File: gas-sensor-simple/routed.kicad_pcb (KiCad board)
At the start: 2 copper layers, 91.4 x 99.1 mm, 43 parts, among them J1 2x5 pin, J2 2x5 socket, J3 2x5 pin, J4 1x2, J5 1x2, J6 1x2, J7 1x2, U1 MQ-8, U10 RG LED, U12 LM393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

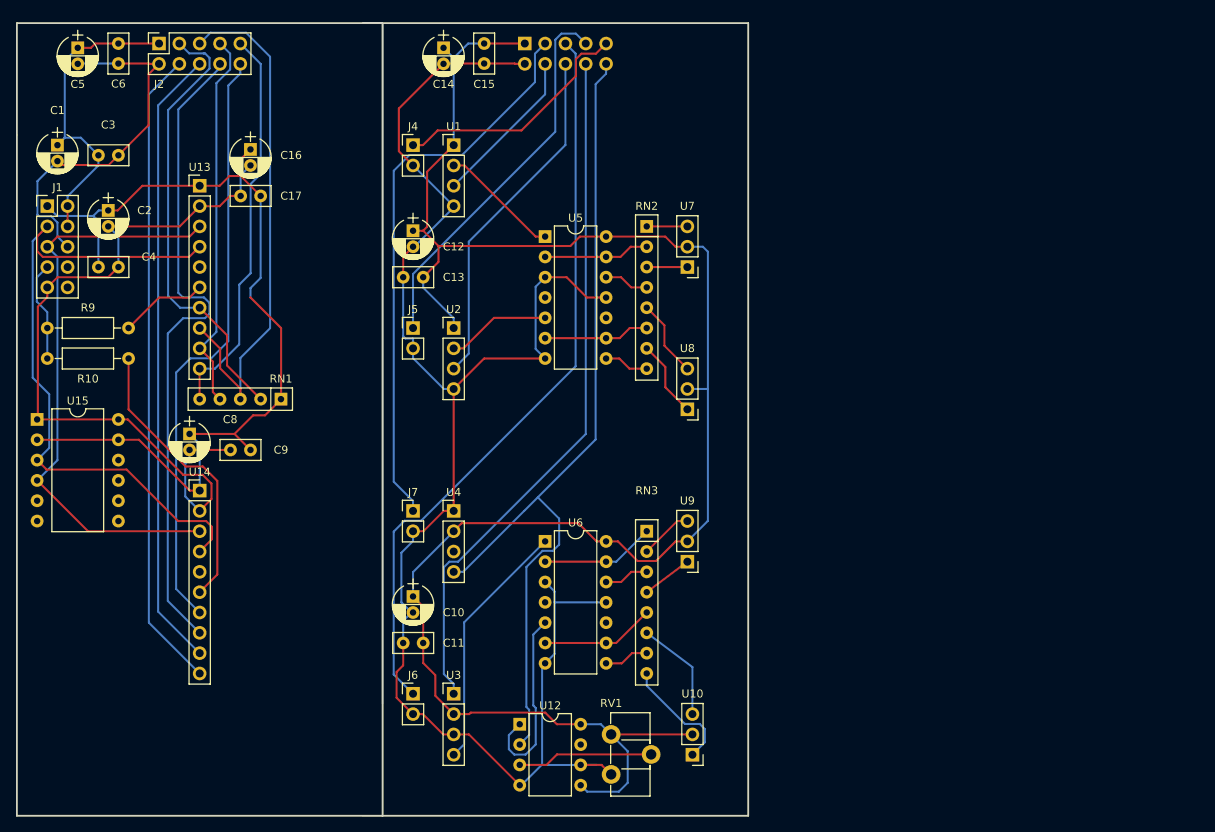
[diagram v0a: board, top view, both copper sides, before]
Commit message: Autorouted version 1 (gas-sensor-simple.kicad_pcb). Start work on version 2 layout (layout.kicad_pcb) moving RPi connector to top of digital board.
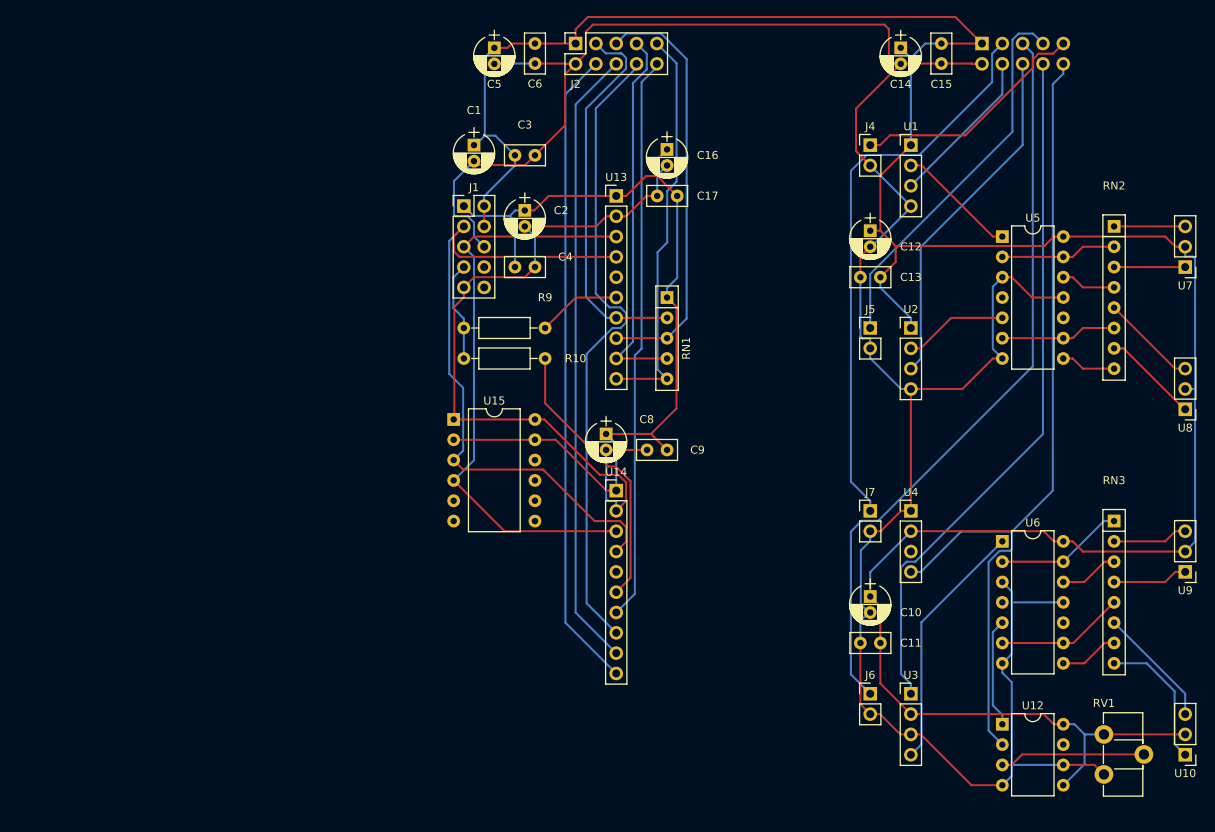
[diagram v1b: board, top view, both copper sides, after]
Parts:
- J1: value 2x5 pin -> RPi
- J2: value 2x5 socket -> digital header
- J3: value 2x5 pin -> digital header
- moved U9 62.2 mm to (248.9, 119.4)
- moved U7 62.2 mm to (248.9, 81.3)
- moved U8 62.2 mm to (248.9, 99.1)
- moved RV1 61.6 mm to (238.8, 139.7)
- moved U10 61.6 mm to (248.9, 142.2)
- moved U12 60.3 mm to (226.1, 138.4)
- moved RN3 58.4 mm to (240.0, 113.0)
- moved RN2 58.4 mm to (240.0, 76.2)
- moved C10 57.2 mm to (209.6, 122.5)
- moved C11 57.2 mm to (208.3, 128.3)
- moved C12 57.2 mm to (209.6, 76.7)
- moved C13 57.2 mm to (208.3, 82.5)
- moved C14 57.2 mm to (213.4, 53.9)
- moved C15 57.2 mm to (218.4, 55.8)
- moved J3 57.2 mm to (223.5, 53.3)
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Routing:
- net VCC: track 269.4 -> 328.1 mm
- net GND: track 251.4 -> 302.6 mm
- net Net-(J2-Pad5): track 65.9 -> 52.9 mm
- net Net-(U12-Pad1): track 23.8 -> 13.7 mm
- net Net-(J2-Pad3): track 55.5 -> 47.7 mm
- net Net-(J2-Pad10): track 74.6 -> 70.7 mm
- net Net-(RN2-Pad3): track 5.08 -> 8.89 mm
- net Net-(RN2-Pad1): track 5.08 -> 8.89 mm
- net +3V3: track 114.9 -> 111.9 mm
- net Net-(RN3-Pad4): track 6.35 -> 9.42 mm
- net Net-(RN3-Pad2): track 6.66 -> 9.42 mm
- net Net-(RN3-Pad8): track 14.9 -> 17.5 mm
- net Net-(RN2-Pad7): track 9.73 -> 12.0 mm
- net Net-(RN2-Pad5): track 9.73 -> 12.0 mm
- net Net-(RN3-Pad6): track 13.0 -> 15.1 mm
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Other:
- board outline removed
- net class Default: trace_width 0.254 -> 0.381
- board text removed: "1.0"
- board text removed: "2017-11-14"
- board text removed: "Analog gas sensor and digital interface"
- board text removed: "Gas Sensor v1"
